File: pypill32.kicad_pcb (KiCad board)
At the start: 2 copper layers, 48.2 x 26.7 mm, 32 parts, among them J1 HeaderR, J2 HeaderL, J3 ISP, U1 SRV05-4, U2 PY32F030F18P6, U3 CH340N

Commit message: intermediate save
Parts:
- removed JP1: PA8_ENA, Jumper:SolderJumper-2_P1.3mm_Open_RoundedPad1.0x1.5mm
- added D3: LED-R, LED_SMD:LED_0805_2012Metric_Pad1.15x1.40mm_HandSolder, F.Cu at (130.9, 70.3)
- added JP2: PA8_SEL, Jumper:SolderJumper-3_P1.3mm_Open_RoundedPad1.0x1.5mm, F.Cu at (130.9, 78.4)
- added R7: 1k, Resistor_SMD:R_0805_2012Metric_Pad1.20x1.40mm_HandSolder, F.Cu at (130.9, 74.1)
- R1: value 1k -> 1.5k
- moved C4 3.94 mm to (128.8, 82.7), turned to -90 degrees
- moved J2 1.37 mm to (101.6, 87.6)
- moved J1 0.36 mm to (101.6, 64.8)
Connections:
- net USB_DM renamed USB_D-
- net USB_DP renamed USB_D+
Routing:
- net /PA8: track 4.37 -> 9.02 mm
- net GND: track 45.7 -> 49.5 mm, vias 68 -> 75
- net Net-(JP2-A): track 0.00 -> 1.97 mm
- net +3V3: track 59.2 -> 61.0 mm
- net Net-(D3-A): track 0.00 -> 1.78 mm
- net Net-(J2-Pin_8): track 10.1 -> 11.7 mm
- net Net-(J2-Pin_7): track 11.2 -> 12.7 mm
- net /PB2: track 7.13 -> 8.48 mm
- net Net-(J2-Pin_9): track 8.42 -> 9.77 mm
- net Net-(J2-Pin_10): track 7.63 -> 8.98 mm
- net Net-(J2-Pin_6): track 19.5 -> 20.8 mm
- net Net-(JP2-C): track 3.93 -> 2.72 mm
- net +5V: track 7.69 -> 6.71 mm, vias 1 -> 0
- net USB_D+: track 18.7 -> 18.1 mm
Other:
- board size 48.2 x 26.7 mm -> 48.2 x 27.2 mm
- board text added: "5V"
- board text added: "BOT"
- board text added: "HZB'24"
- board text added: "PA8/LED"
- board text added: "PWR"
- board text added: "TOP"
- board text removed: "2"
- board text removed: "5"
- board text removed: "L.1"

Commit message: intermediate save
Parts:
- removed J3: ISP, Connector_PinHeader_2.54mm:PinHeader_1x05_P2.54mm_Vertical
- added J4: ISP, Connector_PinHeader_2.54mm:PinHeader_1x04_P2.54mm_Vertical, F.Cu at (135.5, 72.7)
- H1: value MountingHole_Pad_MP -> MountingHole
- moved C2 5.06 mm to (112.6, 81.8)
- moved C5 5.06 mm to (114.8, 81.8)
- moved D3 3.56 mm to (134.4, 69.7), turned to 180 degrees
- moved C11 2.93 mm to (117.9, 78.3)
- moved R6 1.45 mm to (121.1, 78.4)
- moved C1 0.43 mm to (108.0, 70.3)
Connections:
- net /PA13 renamed SWDIO
- net /PA14 renamed SWDCLK
- net Net-(J2-Pin_10) renamed /PA3
- net Net-(J2-Pin_5) renamed /PF0
- net Net-(J2-Pin_6) renamed /PF1
- net Net-(J2-Pin_7) renamed /PF2-NRST
- net Net-(J2-Pin_8) renamed /PF3
- net Net-(J2-Pin_9) renamed /PA2
- H1 pad 1: (no net) -> GND
- H2 pad 1: (no net) -> GND
- H3 pad 1: (no net) -> GND
- H4 pad 1: (no net) -> GND
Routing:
- net SWDCLK: track 13.0 -> 26.7 mm, vias 0 -> 1
- net SWDIO: track 11.0 -> 20.9 mm, vias 0 -> 1
- net GND: track 49.5 -> 56.3 mm, vias 75 -> 85
- net Net-(D3-A): track 1.78 -> 4.99 mm
- net +3V3: track 61.0 -> 62.8 mm, vias 4 -> 3
- net Net-(U3-TXD): track 5.27 -> 6.74 mm
- net /PF0: track 15.9 -> 16.6 mm
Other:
- board text added: "+5V"
- board text added: "/LED"
- board text added: "CLK"
- board text added: "CLK DIO"
- board text added: "DIO"
- board text added: "PA2"
- board text added: "PA3"
- board text added: "PA8"
- board text added: "PB2"
- board text added: "PF0"
- board text added: "PF1"
- board text added: "PF2"
- board text added: "PF3"
- board text added: "SWD"
- board text added: "SWDIO SWDCLK"
- board text added: "USB"
- board text added: "USR"
- board text removed: "PA8/LED"
- board text removed: "PiX PiY PiZ"

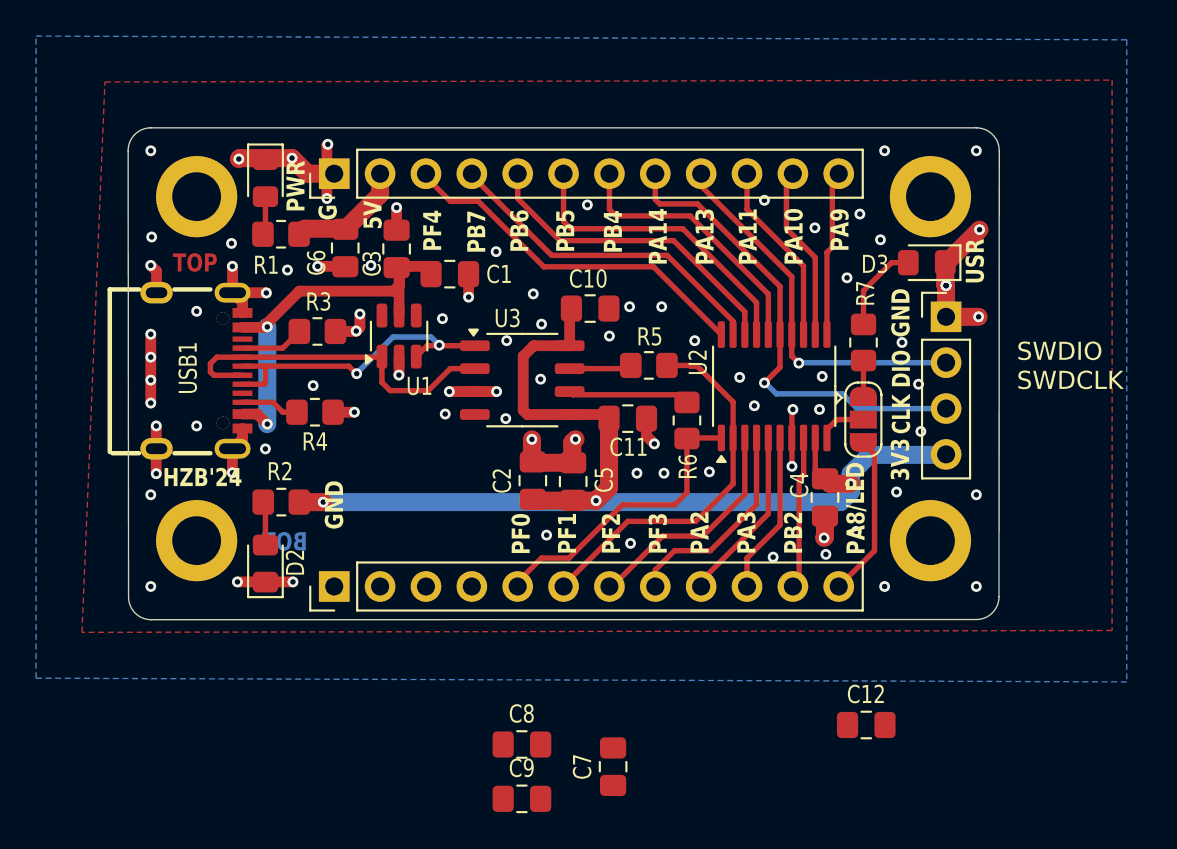
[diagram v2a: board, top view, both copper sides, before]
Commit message: switch footprint and 3d
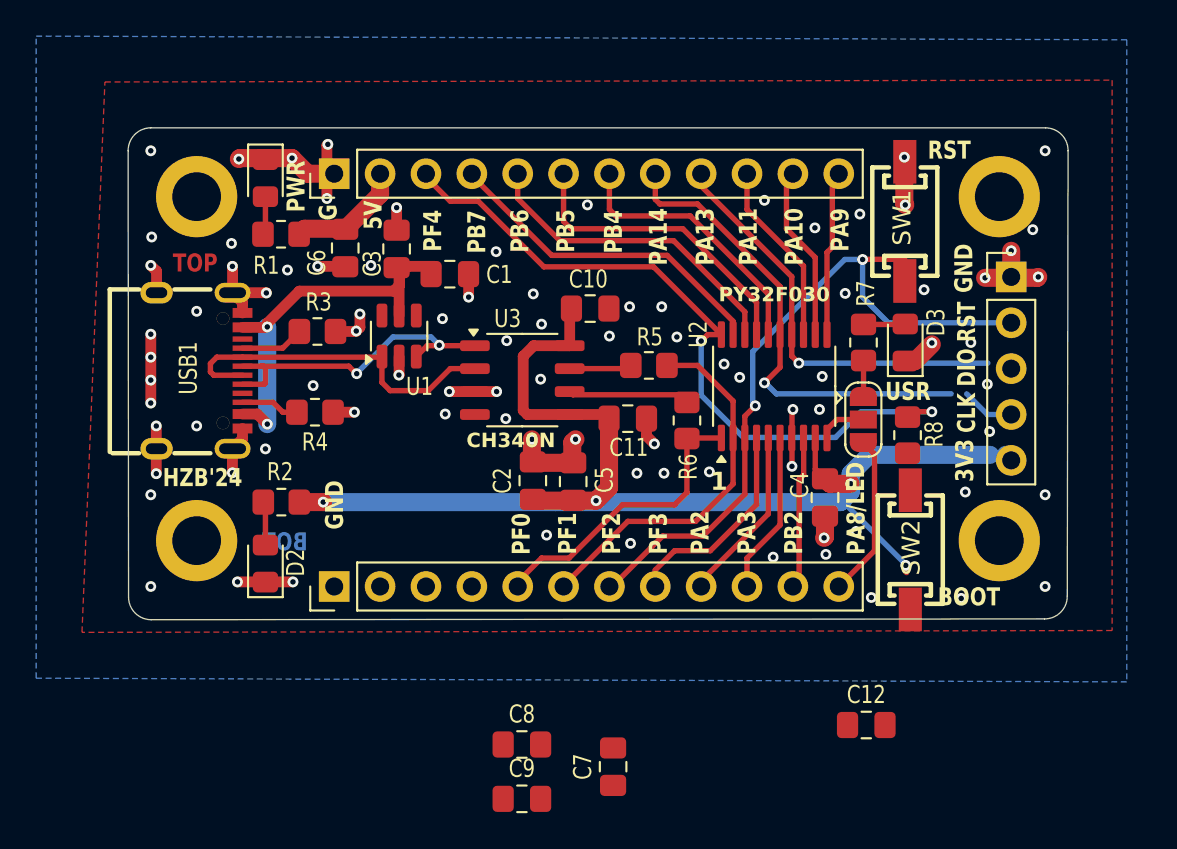
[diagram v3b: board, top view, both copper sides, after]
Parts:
- added R8: 1k, Resistor_SMD:R_0805_2012Metric_Pad1.20x1.40mm_HandSolder, F.Cu at (133.3, 79.2)
- added SW1: SW_Push, pypill32:SW-SMD_L6.0-W3.5-LS8.2, F.Cu at (133.2, 67.4)
- added SW2: SW_Push, pypill32:SW-SMD_L6.0-W3.5-LS8.2, F.Cu at (133.5, 85.6)
- J4: footprint Connector_PinHeader_2.54mm:PinHeader_1x04_P2.54mm_Vertical -> Connector_PinHeader_2.54mm:PinHeader_1x05_P2.54mm_Vertical
- moved D3 4.58 mm to (133.2, 74.1), turned to 90 degrees
- moved J4 4.23 mm to (139.1, 70.5)
- moved H1 3.81 mm to (138.4, 66.0)
- moved H2 3.81 mm to (138.4, 85.1)
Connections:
- net /PF4 renamed BOOT0
- H1 pad 1: GND -> (no net)
- H2 pad 1: GND -> (no net)
- H3 pad 1: GND -> (no net)
- H4 pad 1: GND -> (no net)
- J2 pad 7: /PF2-NRST -> NRST
- J4 pad 2: SWDIO -> NRST
- J4 pad 3: SWDCLK -> SWDIO
- J4 pad 4: +3V3 -> SWDCLK
- U2 pad 3: /PF2-NRST -> NRST
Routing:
- net NRST: track 0.00 -> 38.4 mm, vias 0 -> 2
- net BOOT0: track 20.2 -> 40.2 mm, vias 0 -> 2
- net /PF2-NRST: track 12.7 -> 0.00 mm
- net +3V3: track 62.8 -> 71.2 mm, vias 3 -> 4
- net SWDCLK: track 26.7 -> 29.5 mm
- net SWDIO: track 20.9 -> 23.6 mm
- net Net-(D3-A): track 4.99 -> 2.32 mm
- net GND: track 56.3 -> 57.8 mm, vias 85 -> 88
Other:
- board size 48.2 x 27.2 mm -> 52.1 x 27.2 mm
- board text added: "1"
- board text added: "BOOT"
- board text added: "CH340N"
- board text added: "CLK DIO RST"
- board text added: "PY32F030"
- board text added: "RST"
- board text removed: "CLK DIO"
- board text removed: "SWDIO SWDCLK"

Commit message: some progress
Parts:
- added REF**: OSHW-Symbol_6.7x6mm_SilkScreen, Symbol:OSHW-Symbol_6.7x6mm_SilkScreen, B.Cu at (127.3, 77.0)
- added REF**: ESD-Logo_6.6x6mm_SilkScreen, Symbol:ESD-Logo_6.6x6mm_SilkScreen, B.Cu at (101.3, 78.1)
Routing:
- net GND: vias 88 -> 87
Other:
- board text added: "USB-C"
- board text removed: "USB"

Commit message: to be continued
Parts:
- removed C8: 100nF, Capacitor_SMD:C_0805_2012Metric_Pad1.18x1.45mm_HandSolder
- H2, H3, H4: value MountingHole_Pad_MP -> MountingHole
- SW1: value SW_Push -> RST_BTN
- SW2: value SW_Push -> BOOT_BTN
- moved C7 31.9 mm to (103.3, 68.8), turned to -90 degrees
- moved C12 30.0 mm to (104.2, 81.9), turned to 90 degrees
- moved C9 22.5 mm to (100.6, 80.0)
- moved H2 1.27 mm to (138.3, 86.4)
- moved H4 1.27 mm to (94.0, 86.4)
- moved C1 1.12 mm to (109.1, 70.2)
- moved C3 1.07 mm to (106.1, 68.9)
- moved C6 0.87 mm to (101.3, 68.8)
- moved R1 0.79 mm to (98.0, 68.6)
- moved J4 0.15 mm to (138.9, 70.5)
- moved H1 0.10 mm to (138.3, 66.0)
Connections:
- H1 pad 1: (no net) -> GND
- H2 pad 1: (no net) -> GND
- H3 pad 1: (no net) -> GND
- H4 pad 1: (no net) -> GND
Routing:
- net VBUS: track 21.9 -> 25.0 mm
- net +5V: track 6.71 -> 8.83 mm
- net GND: track 57.8 -> 59.9 mm, vias 87 -> 90
- net +3V3: track 71.2 -> 73.2 mm
- net SWDIO: track 23.6 -> 24.9 mm
- net Net-(D1-A): track 2.14 -> 2.90 mm
- net SWDCLK: track 29.5 -> 30.3 mm
- net NRST: track 38.4 -> 39.1 mm
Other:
- board size 52.1 x 27.2 mm -> 50.8 x 27.9 mm
- board text removed: "+5V"
- board text removed: "CH340N"
- board text removed: "CLK"
- board text removed: "DIO"
- board text removed: "PA10"
- board text removed: "PA11"
- board text removed: "PA13"
- board text removed: "PA14"
- board text removed: "PB4"
- board text removed: "PB5"
- board text removed: "PB6"
- board text removed: "PB7"
- board text removed: "PF4"

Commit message: silks and some routing, to be continued
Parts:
- added C13: 12p TSEKKAA, Capacitor_SMD:C_0805_2012Metric_Pad1.18x1.45mm_HandSolder, B.Cu at (131.8, 72.7)
- added C8: 12p TSEKKAA, Capacitor_SMD:C_0805_2012Metric_Pad1.18x1.45mm_HandSolder, B.Cu at (127.3, 72.2)
- added Y1: 32.768 kHz, Crystal:Crystal_Round_D2.0mm_Vertical, F.Cu at (130.4, 70.6)
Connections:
- D2 pad 2: Net-(D2-A) -> PWRLED
- J2 pad 2: unconnected-(J2-Pin_2-Pad2) -> PWRLED
- J2 pad 3: unconnected-(J2-Pin_3-Pad3) -> +3V3
- J2 pad 4: unconnected-(J2-Pin_4-Pad4) -> GND
- R2 pad 2: Net-(D2-A) -> PWRLED
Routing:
- net PWRLED: track 0.00 -> 10.8 mm
- net +3V3: track 73.2 -> 78.7 mm
- net GND: track 59.9 -> 64.2 mm, vias 90 -> 95
- net /PA9: track 9.18 -> 12.5 mm
- net NRST: track 39.1 -> 41.6 mm
- net Net-(D2-A): track 2.43 -> 0.00 mm
- net Net-(R8-Pad1): track 0.07 -> 2.19 mm
- net /PA10: track 9.72 -> 11.4 mm
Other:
- board text added: "CLK"
- board text added: "DIO"
- board text added: "PA10"
- board text added: "PA11"
- board text added: "PA13"
- board text added: "PA14"
- board text added: "PB4"
- board text added: "PB5"
- board text added: "PB6"
- board text added: "PB7"
- board text added: "PF2/RST"
- board text added: "PWR LED"
- board text removed: "CLK DIO RST"
- board text removed: "PF2"
- board text removed: "PY32F030"

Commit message: further
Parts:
- removed D1: LED-G, LED_SMD:LED_0805_2012Metric_Pad1.15x1.40mm_HandSolder
- removed R1: 1.5k, Resistor_SMD:R_0805_2012Metric_Pad1.20x1.40mm_HandSolder
- added C14: 10uF, Capacitor_SMD:C_0805_2012Metric_Pad1.18x1.45mm_HandSolder, B.Cu at (107.5, 69.5)
- added C15: 100nF, Capacitor_SMD:C_0805_2012Metric_Pad1.18x1.45mm_HandSolder, B.Cu at (115.1, 74.5)
- added F1: 0.8A, Fuse:Fuse_1206_3216Metric_Pad1.42x1.75mm_HandSolder, F.Cu at (99.5, 69.4)
- added FB1: ~, Inductor_SMD:L_1206_3216Metric_Pad1.42x1.75mm_HandSolder, F.Cu at (103.2, 68.0)
- added U4: AMS1117-3.3, Package_TO_SOT_SMD:SOT-223-3_TabPin2, F.Cu at (109.7, 81.0)
- C1, C12, C2, C5, C6, C7: moved to B.Cu
- moved C12 15.4 mm to (119.6, 81.3)
- moved C7 9.28 mm to (112.5, 70.0)
- moved C1 8.73 mm to (100.5, 71.5)
- moved C5 6.32 mm to (108.5, 81.8)
- moved C6 4.17 mm to (105.5, 69.4)
- moved R6 3.07 mm to (118.9, 76.4), turned to 0 degrees
- moved C10 2.11 mm to (117.9, 72.3)
- moved C2 2.01 mm to (110.6, 81.8)
- moved C11 1.68 mm to (116.2, 78.3)
- moved U3 1.60 mm to (111.9, 74.6)
- moved C3 1.42 mm to (106.6, 70.3), turned to 0 degrees
- moved R4 1.12 mm to (101.7, 78.0)
- moved R5 0.98 mm to (118.9, 74.4)
- moved J4 0.41 mm to (139.3, 70.5)
- moved D2 0.15 mm to (97.9, 86.4)
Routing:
- net GND: track 64.2 -> 100.4 mm, vias 95 -> 120
- net +5V: track 8.83 -> 33.6 mm, vias 0 -> 2
- net +3V3: track 78.7 -> 86.3 mm, vias 4 -> 3
- net /PF0: track 16.6 -> 20.2 mm
- net Net-(U3-TXD): track 6.74 -> 3.78 mm
- net Net-(D1-A): track 2.90 -> 0.00 mm
- net Net-(F1-Pad2): track 0.00 -> 2.40 mm
- net USB_D-: track 19.2 -> 20.4 mm
- net Net-(USB1-CC2): track 3.24 -> 4.36 mm
- net USB_D+: track 18.1 -> 18.9 mm
- net /PF1: track 20.8 -> 21.4 mm
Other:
- board size 50.8 x 27.9 mm -> 52.1 x 27.9 mm
- board text added: "B0"
- board text added: "BOTTOM"
- board text added: "F0"
- board text added: "FUSE"
- board text added: "HZB '24"
- board text added: "P"
- board text added: "PA13=SWDIO"
- board text added: "PA14=SWCLK"
- board text added: "RST/PF2"
- board text added: "SWCLK"
- board text added: "SWDIO"
- board text added: "Xtal"
- board text removed: "BOT"
- board text removed: "PWR"
- board text removed: "USB-C"

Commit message: almost ready
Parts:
- removed the REF** at (127.3, 77.0)
- added C16: 10uF, Capacitor_SMD:C_0805_2012Metric_Pad1.18x1.45mm_HandSolder, B.Cu at (106.5, 81.8)
- added OHW: OSHW-Symbol_6.7x6mm_SilkScreen, Symbol:OSHW-Symbol_6.7x6mm_SilkScreen, B.Cu at (102.1, 75.0)
- moved REF** 8.57 mm to (94.1, 73.4)
- moved D2 5.28 mm to (94.2, 82.7), turned to 0 degrees
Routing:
- net +3V3: track 86.3 -> 88.1 mm
- net PWRLED: track 10.7 -> 12.4 mm, vias 0 -> 1
- net GND: track 100.4 -> 100.7 mm, vias 120 -> 134
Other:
- board text added: "8kB/64kB"
- board text added: "ESD"
- board text added: "LL '24"
- board text added: "Open HW: CERN OHL"
- board text added: "PWR"
- board text added: "b0"
- board text added: "reg."
- board text removed: "B0"
- board text removed: "HZB '24"
- board text removed: "HZB'24"
- board text removed: "P"
